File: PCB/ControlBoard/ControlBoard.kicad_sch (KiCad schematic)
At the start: 44 parts, among them J1 LINK-A, J10 Conn_01x08, J2 LINK-B, J3 Conn_01x04, J4 PortA, J5 PortB, J6 PortC, J7 ICSPDAT/VO, J8 ICSP, J9 Conn_01x08, Q1 Q_NMOS_GSD, Q2 Q_NMOS_GSD, U1 TPS259630, U2 PIC18F57Q84, U3 MCP2551-I-SN

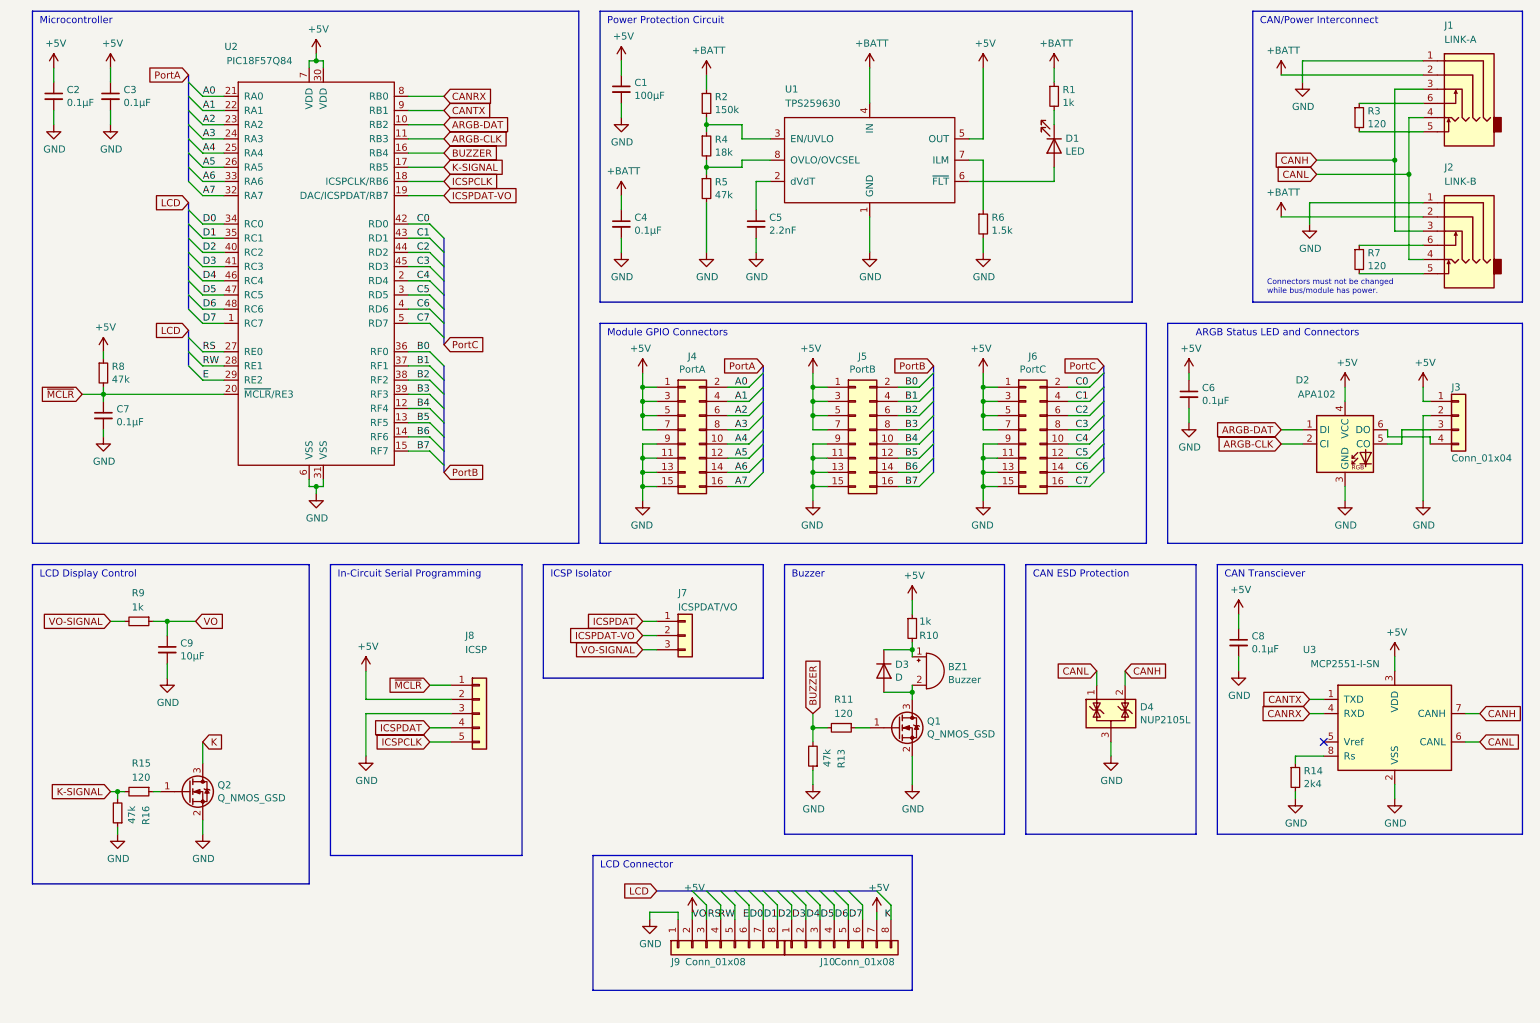
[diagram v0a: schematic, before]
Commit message: Add operator module, fix issue with time display when timer runs out.
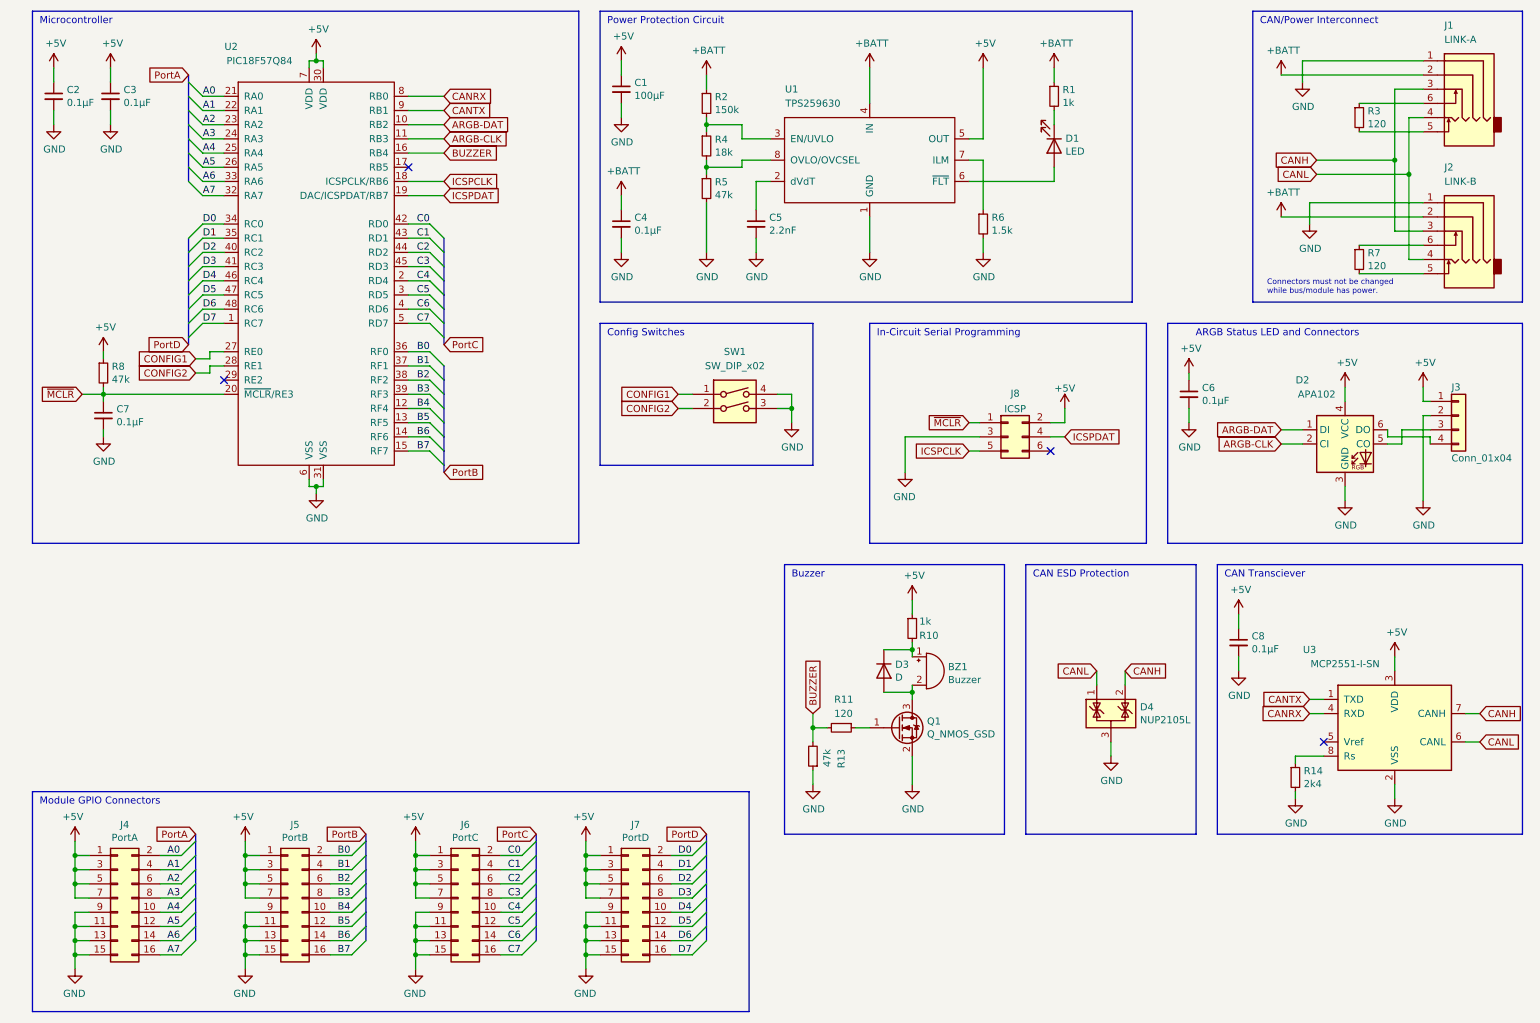
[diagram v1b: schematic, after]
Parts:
- removed C9: 10μF, Capacitor_SMD:C_0805_2012Metric, symbol Device:C_Small
- removed J10, J9: Conn_01x08, Connector_JST:JST_XH_B8B-XH-A_1x08_P2.50mm_Vertical, symbol Connector_Generic:Conn_01x08
- removed J7: ICSPDAT/VO, Connector_PinHeader_2.54mm:PinHeader_1x03_P2.54mm_Vertical, symbol Connector_Generic:Conn_01x03
- removed J8: ICSP, Connector_PinHeader_2.54mm:PinHeader_1x05_P2.54mm_Vertical, symbol Connector_Generic:Conn_01x05
- removed Q2: Q_NMOS_GSD, Package_TO_SOT_SMD:SOT-23, symbol Device:Q_NMOS_GSD
- removed R15: 120, Resistor_SMD:R_0805_2012Metric, symbol Device:R_Small
- removed R16: 47k, Resistor_SMD:R_0805_2012Metric, symbol Device:R_Small
- removed R9: 1k, Resistor_SMD:R_0805_2012Metric, symbol Device:R_Small
- added J7: PortD, Custom:PinHeader_2x08_P2.54mm_Vertical-Centered, symbol Connector_Generic:Conn_02x08_Odd_Even
- added J8: ICSP, Connector:Tag-Connect_TC2030-IDC-NL_2x03_P1.27mm_Vertical, symbol Connector_Generic:Conn_02x03_Odd_Even
- added SW1: SW_DIP_x02, Button_Switch_SMD:SW_DIP_SPSTx02_Slide_6.7x6.64mm_W8.61mm_P2.54mm_LowProfile, symbol Switch:SW_DIP_x02
- BZ1: footprint Custom:MultisizeBuzzer -> Buzzer_Beeper:MagneticBuzzer_CUI_CMT-8504-100-SMT
- C1: footprint Capacitor_THT:CP_Radial_D6.3mm_P2.50mm -> Capacitor_Tantalum_SMD:CP_EIA-7343-31_Kemet-D
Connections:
- net ICSPDAT-VO is gone; now on net ICSPDAT: U2.19 (DAC/ICSPDAT/RB7)
- net +5V: now also J7.1 (Pin_1), J7.3 (Pin_3), J7.5 (Pin_5), J7.7 (Pin_7), J8.2 (Pin_2)
- net D0: now also J7.2 (Pin_2)
- net D1: now also J7.4 (Pin_4)
- net D2: now also J7.6 (Pin_6)
- net D3: now also J7.8 (Pin_8)
- net D4: now also J7.10 (Pin_10)
- net D5: now also J7.12 (Pin_12)
- net D6: now also J7.14 (Pin_14)
- net D7: now also J7.16 (Pin_16)
- net GND: now also J7.11 (Pin_11), J7.13 (Pin_13), J7.15 (Pin_15), J7.9 (Pin_9), J8.3 (Pin_3), SW1.3, SW1.4
- net ICSPCLK: now also J8.5 (Pin_5)
- net ICSPDAT: now also J8.4 (Pin_4)
- net ~{MCLR}: now also J8.1 (Pin_1)
- net E: no longer names the net of U2.29 (RE2)
- net K-SIGNAL: no longer names the net of U2.17 (RB5)
- net RS renamed CONFIG1
- net CONFIG1: now also SW1.1
- net RW renamed CONFIG2
- net CONFIG2: now also SW1.2
- no-connect marks 1 -> 4
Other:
- note added: "Config Switches"
- note removed: "ICSP Isolator"
- note removed: "LCD Connector"
- note removed: "LCD Display Control"
- moved on the sheet: J4, J5, J6

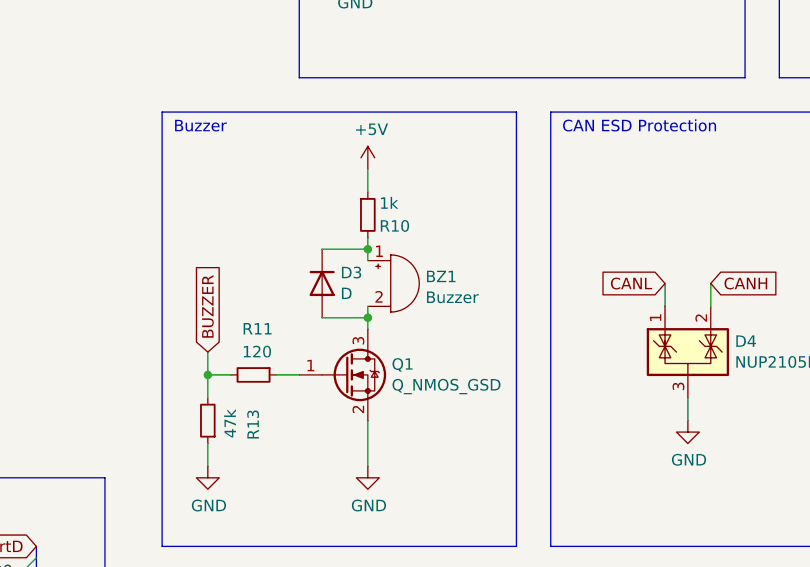
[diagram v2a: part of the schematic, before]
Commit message: Upgrade KiCad files from 6.0 to 7.0.
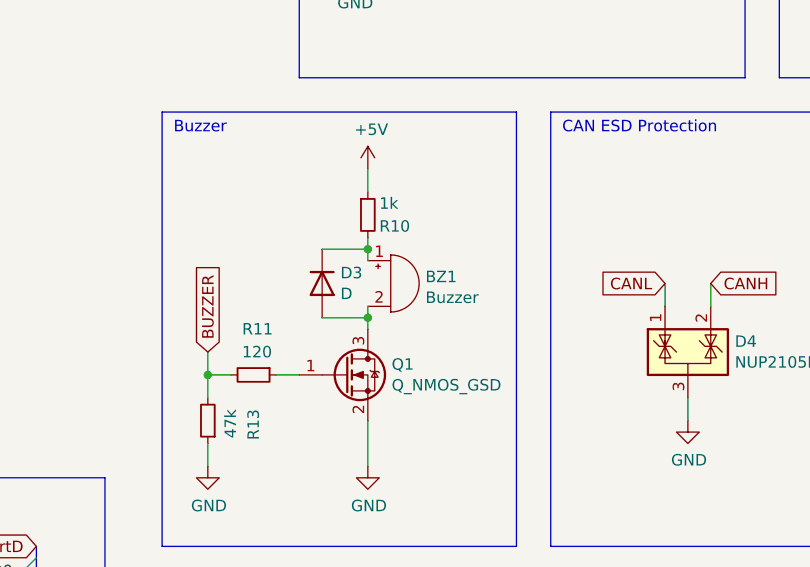
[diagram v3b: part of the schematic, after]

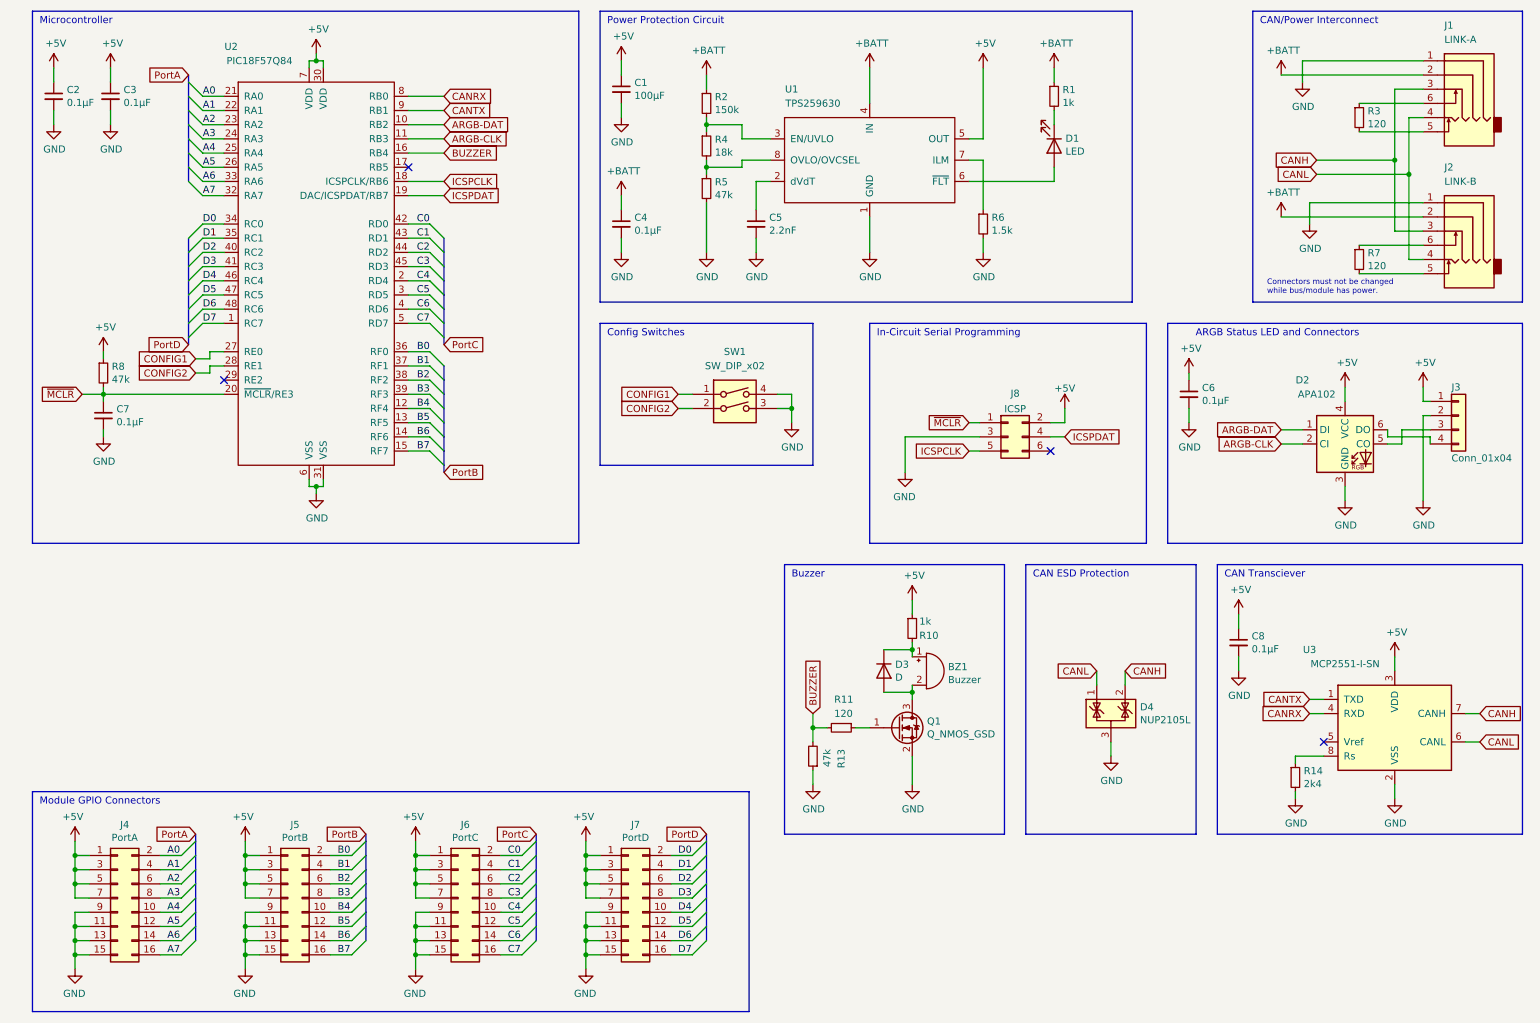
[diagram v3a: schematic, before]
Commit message: Beginning rework of Control Board for respin.
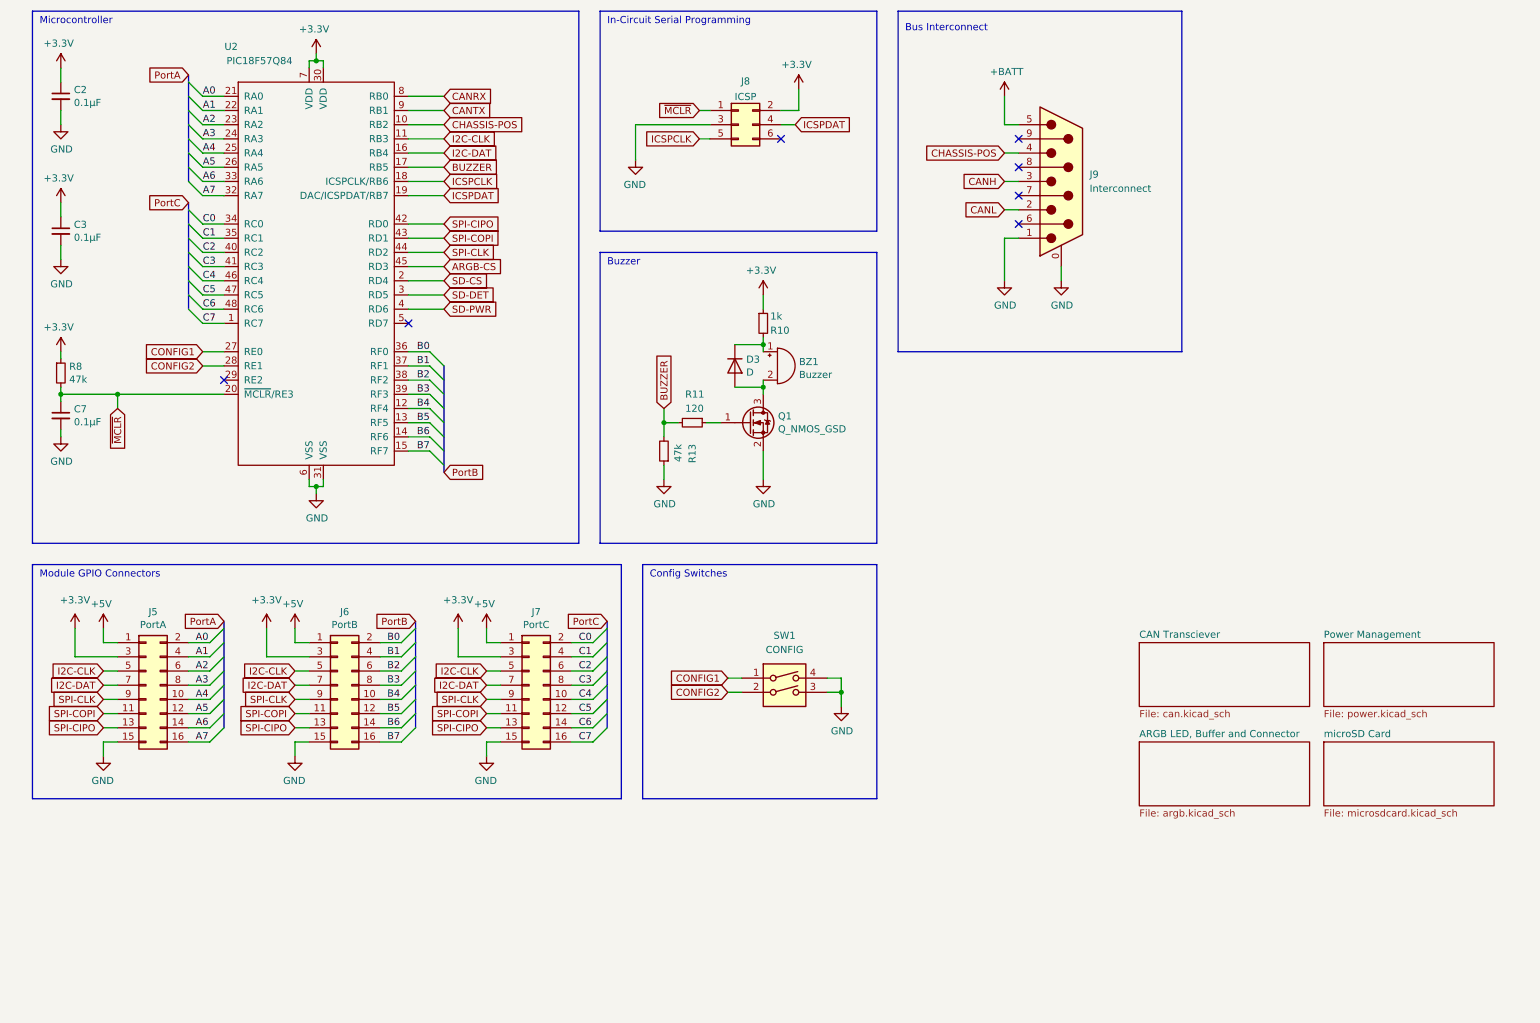
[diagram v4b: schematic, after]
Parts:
- removed C1: 100μF, Capacitor_Tantalum_SMD:CP_EIA-7343-31_Kemet-D, symbol Device:C_Small
- removed C4, C6, C8: 0.1μF, Capacitor_SMD:C_0805_2012Metric, symbol Device:C_Small
- removed C5: 2.2nF, Capacitor_SMD:C_0805_2012Metric, symbol Device:C_Small
- removed D1: LED, LED_SMD:LED_0805_2012Metric, symbol Device:LED
- removed D2: APA102, LED_SMD:LED_RGB_5050-6, symbol LED:APA102
- removed D4: NUP2105L, Package_TO_SOT_SMD:SOT-23, symbol Power_Protection:NUP2105L
- removed J1: LINK-A, Connector_Audio:Jack_3.5mm_PJ311_Horizontal, symbol KTANE:AudioJack4_SwitchTR1
- removed J2: LINK-B, Connector_Audio:Jack_3.5mm_PJ311_Horizontal, symbol KTANE:AudioJack4_SwitchTR1
- removed J3: Conn_01x04, Connector_JST:JST_PH_B4B-PH-SM4-TB_1x04-1MP_P2.00mm_Vertical, symbol Connector_Generic:Conn_01x04
- removed J4: PortA, Custom:PinHeader_2x08_P2.54mm_Vertical-Centered, symbol Connector_Generic:Conn_02x08_Odd_Even
- removed R1: 1k, Resistor_SMD:R_0805_2012Metric, symbol Device:R_Small
- removed R14: 2k4, Resistor_SMD:R_0805_2012Metric, symbol Device:R_Small
- removed R2: 150k, Resistor_SMD:R_0805_2012Metric, symbol Device:R_Small
- removed R3, R7: 120, Resistor_SMD:R_0805_2012Metric, symbol Device:R_Small
- removed R4: 18k, Resistor_SMD:R_0805_2012Metric, symbol Device:R_Small
- removed R5: 47k, Resistor_SMD:R_0805_2012Metric, symbol Device:R_Small
- removed R6: 1.5k, Resistor_SMD:R_0805_2012Metric, symbol Device:R_Small
- removed U1: TPS259630, Package_SO:SOIC-8-1EP_3.9x4.9mm_P1.27mm_EP2.29x3mm, symbol KTANE:TPS25962X
- removed U3: MCP2551-I-SN, Package_SO:SOIC-8_3.9x4.9mm_P1.27mm, symbol Interface_CAN_LIN:MCP2551-I-SN
- added J9: Interconnect, symbol Connector:DE9_Plug_MountingHoles
- J5: value PortB -> PortA
- J6: value PortC -> PortB
- J7: value PortD -> PortC
- SW1: value SW_DIP_x02 -> CONFIG
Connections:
- net D0 is gone; now on net C0: J7.2 (Pin_2), U2.34 (RC0)
- net D1 is gone; now on net C1: J7.4 (Pin_4), U2.35 (RC1)
- net D2 is gone; now on net C2: J7.6 (Pin_6), U2.40 (RC2)
- net D3 is gone; now on net C3: J7.8 (Pin_8), U2.41 (RC3)
- net D4 is gone; now on net C4: J7.10 (Pin_10), U2.46 (RC4)
- net D5 is gone; now on net C5: J7.12 (Pin_12), U2.47 (RC5)
- net D6 is gone; now on net C6: J7.14 (Pin_14), U2.48 (RC6)
- net D7 is gone; now on net C7: J7.16 (Pin_16), U2.1 (RC7)
- net +5V: no longer C2.1, C3.1, J5.3 (Pin_3), J5.5 (Pin_5), J5.7 (Pin_7), J6.3 (Pin_3), J6.5 (Pin_5), J6.7 (Pin_7), J7.3 (Pin_3), J7.5 (Pin_5), J7.7 (Pin_7), J8.2 (Pin_2), R10.1, R8.1, U2.30 (VDD), U2.7 (VDD)
- net +BATT: now also J9.5
- net A0: now also J5.2 (Pin_2)
- net A1: now also J5.4 (Pin_4)
- net A2: now also J5.6 (Pin_6)
- net A3: now also J5.8 (Pin_8)
- net A4: now also J5.10 (Pin_10)
- net A5: now also J5.12 (Pin_12)
- net A6: now also J5.14 (Pin_14)
- net A7: now also J5.16 (Pin_16)
- net B0: now also J6.2 (Pin_2); no longer J5.2 (Pin_2)
- net B1: now also J6.4 (Pin_4); no longer J5.4 (Pin_4)
- net B2: now also J6.6 (Pin_6); no longer J5.6 (Pin_6)
- net B3: now also J6.8 (Pin_8); no longer J5.8 (Pin_8)
- net B4: now also J6.10 (Pin_10); no longer J5.10 (Pin_10)
- net B5: now also J6.12 (Pin_12); no longer J5.12 (Pin_12)
- net B6: now also J6.14 (Pin_14); no longer J5.14 (Pin_14)
- net B7: now also J6.16 (Pin_16); no longer J5.16 (Pin_16)
- net BUZZER: now also U2.17 (RB5); no longer U2.16 (RB4)
- net C0: no longer J6.2 (Pin_2), U2.42 (RD0)
- net C1: no longer J6.4 (Pin_4), U2.43 (RD1)
- net C2: no longer J6.6 (Pin_6), U2.44 (RD2)
- net C3: no longer J6.8 (Pin_8), U2.45 (RD3)
- net C4: no longer J6.10 (Pin_10), U2.2 (RD4)
- net C5: no longer J6.12 (Pin_12), U2.3 (RD5)
- net C6: no longer J6.14 (Pin_14), U2.4 (RD6)
- net C7: no longer J6.16 (Pin_16), U2.5 (RD7)
- net CANH: now also J9.3
- net CANL: now also J9.2
- net GND: now also J9.0 (PAD), J9.1; no longer J5.11 (Pin_11), J5.13 (Pin_13), J5.9 (Pin_9), J6.11 (Pin_11), J6.13 (Pin_13), J6.9 (Pin_9), J7.11 (Pin_11), J7.13 (Pin_13), J7.9 (Pin_9)
- net ARGB-CLK renamed I2C-CLK
- net I2C-CLK: now also J5.5 (Pin_5), J6.5 (Pin_5), J7.5 (Pin_5)
- net ARGB-DAT renamed CHASSIS-POS
- net CHASSIS-POS: now also J9.4
- new net +3.3V: C2.1, C3.1, J5.3 (Pin_3), J6.3 (Pin_3), J7.3 (Pin_3), J8.2 (Pin_2), R10.1, R8.1, U2.30 (VDD), U2.7 (VDD)
- new net ARGB-CS: U2.45 (RD3)
- new net I2C-DAT: J5.7 (Pin_7), J6.7 (Pin_7), J7.7 (Pin_7), U2.16 (RB4)
- new net SD-CS: U2.2 (RD4)
- new net SD-DET: U2.3 (RD5)
- new net SD-PWR: U2.4 (RD6)
- new net SPI-CIPO: J5.13 (Pin_13), J6.13 (Pin_13), J7.13 (Pin_13), U2.42 (RD0)
- new net SPI-CLK: J5.9 (Pin_9), J6.9 (Pin_9), J7.9 (Pin_9), U2.44 (RD2)
- new net SPI-COPI: J5.11 (Pin_11), J6.11 (Pin_11), J7.11 (Pin_11), U2.43 (RD1)
- no-connect marks 4 -> 7
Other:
- added sheet ARGB LED, Buffer and Connector (argb.kicad_sch)
- added sheet CAN Transciever (can.kicad_sch)
- added sheet Power Management (power.kicad_sch)
- added sheet microSD Card (microsdcard.kicad_sch)
- note added: "Bus Interconnect"
- note removed: "ARGB Status LED and Connectors"
- note removed: "CAN ESD Protection"
- note removed: "CAN Transciever"
- note removed: "CAN/Power Interconnect"
- note removed: "Connectors must not be changed while bus/module has power."
- note removed: "Power Protection Circuit"
- moved on the sheet: BZ1, C2, C3, C7, D3, J5, J6, J7, J8, Q1, R10, R11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
